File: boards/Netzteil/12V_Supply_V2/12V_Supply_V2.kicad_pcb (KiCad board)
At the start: 2 copper layers, 90 x 66 mm, 52 parts, among them P1 12V_AC, P2 12V_DC_1, P3 12V_DC_2, P4 Relais, P5 12V_DC_3, P6 12V_DC_4, P7 Relais, Q1 BS170, U1 LM393, U2 LM7812CT

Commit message: Added Power LEDs
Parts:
- added D12: LED, LED_THT:LED_D3.0mm, F.Cu at (167.9, 58.7)
- added R2: 47k, Resistor_THT:R_Axial_DIN0207_L6.3mm_D2.5mm_P10.16mm_Horizontal, F.Cu at (162.6, 62.5)
- moved C1 4.83 mm to (140.7, 68.1)
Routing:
- net Net-(D12-Pad2): track 0.00 -> 7.80 mm
- net +12V: track 147.7 -> 154.8 mm
- net GND: vias 29 -> 28
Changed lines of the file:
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@@
     (thickness 1.6)
     (drawings 7)
-    (tracks 155)
+    (tracks 159)
     (zones 0)
-    (modules 52)
-    (nets 19)
+    (modules 54)
+    (nets 20)
   )
   (page A4)
@@
   )
   (setup
-    (last_trace_width 0.5)
+    (last_trace_width 1)
     (user_trace_width 0.5)
     (user_trace_width 1)
@@
   (net 17 "Net-(C10-Pad2)")
   (net 18 "Net-(C11-Pad2)")
+  (net 19 "Net-(D12-Pad2)")
   (net_class Default "Dies ist die voreingestellte Netzklasse."
     (clearance 0.2)
@@
     (add_net "Net-(C4-Pad1)")
     (add_net "Net-(C7-Pad1)")
+    (add_net "Net-(D12-Pad2)")
     (add_net "Net-(D3-Pad1)")
     (add_net "Net-(D5-Pad1)")
@@
     (diff_pair_gap 0.25)
   )
+  (module Resistor_THT:R_Axial_DIN0207_L6.3mm_D2.5mm_P10.16mm_Horizontal (layer F.Cu)
+    (at 162.56 62.484 90)
+    (descr "Resistor, Axial_DIN0207 series, Axial, Horizontal, pin pitch=10.16mm, 0.25W = 1/4W, length*diameter=6.3*2.5mm^2, http://cdn-reichelt.de/documents/datenblatt/B400/1_4W%23YAG.pdf")
+    (tags "Resistor Axial_DIN0207 series Axial Horizontal pin pitch 10.16mm 0.25W = 1/4W length 6.3mm diameter 2.5mm")
+    (fp_text reference R2 (at 5.08 -2.37 90) (layer F.SilkS)
+      (effects (font (size 1 1) (thickness 0.15)))
+    )
+    (fp_text value 47k (at 5.08 2.37 90) (layer F.Fab)
+      (effects (font (size 1 1) (thickness 0.15)))
+    )
+    (fp_text user %R (at 5.08 0 90) (layer F.Fab)
+      (effects (font (size 1 1) (thickness 0.15)))
+    )
+    (fp_line (start 11.21 -1.5) (end -1.05 -1.5) (layer F.CrtYd) (width 0.05))
+    (fp_line (start 11.21 1.5) (end 11.21 -1.5) (layer F.CrtYd) (width 0.05))
+    (fp_line (start -1.05 1.5) (end 11.21 1.5) (layer F.CrtYd) (width 0.05))
+    (fp_line (start -1.05 -1.5) (end -1.05 1.5) (layer F.CrtYd) (width 0.05))
+    (fp_line (start 9.12 0) (end 8.35 0) (layer F.SilkS) (width 0.12))
+    (fp_line (start 1.04 0) (end 1.81 0) (layer F.SilkS) (width 0.12))
+    (fp_line (start 8.35 -1.37) (end 1.81 -1.37) (layer F.SilkS) (width 0.12))
+    (fp_line (start 8.35 1.37) (end 8.35 -1.37) (layer F.SilkS) (width 0.12))
+    (fp_line (start 1.81 1.37) (end 8.35 1.37) (layer F.SilkS) (width 0.12))
+    (fp_line (start 1.81 -1.37) (end 1.81 1.37) (layer F.SilkS) (width 0.12))
+    (fp_line (start 10.16 0) (end 8.23 0) (layer F.Fab) (width 0.1))
+    (fp_line (start 0 0) (end 1.93 0) (layer F.Fab) (width 0.1))
+    (fp_line (start 8.23 -1.25) (end 1.93 -1.25) (layer F.Fab) (width 0.1))
+    (fp_line (start 8.23 1.25) (end 8.23 -1.25) (layer F.Fab) (width 0.1))
+    (fp_line (start 1.93 1.25) (end 8.23 1.25) (layer F.Fab) (width 0.1))
+    (fp_line (start 1.93 -1.25) (end 1.93 1.25) (layer F.Fab) (width 0.1))
+    (pad 2 thru_hole oval (at 10.16 0 90) (size 1.6 1.6) (drill 0.8) (layers *.Cu *.Mask)
+      (net 19 "Net-(D12-Pad2)"))
+    (pad 1 thru_hole circle (at 0 0 90) (size 1.6 1.6) (drill 0.8) (layers *.Cu *.Mask)
+      (net 3 +12V))
+    (model ${KISYS3DMOD}/Resistor_THT.3dshapes/R_Axial_DIN0207_L6.3mm_D2.5mm_P10.16mm_Horizontal.wrl
+      (at (xyz 0 0 0))
+      (scale (xyz 1 1 1))
+      (rotate (xyz 0 0 0))
+    )
+  )
+  (module LED_THT:LED_D3.0mm (layer F.Cu)
+    (at 167.894 58.674 90)
+    (descr "LED, diameter 3.0mm, 2 pins")
+    (tags "LED diameter 3.0mm 2 pins")
+    (fp_text reference D12 (at 1.27 -2.96 90) (layer F.SilkS)
+      (effects (font (size 1 1) (thickness 0.15)))
+    )
+    (fp_text value LED (at 1.27 2.96 90) (layer F.Fab)
+      (effects (font (size 1 1) (thickness 0.15)))
+    )
+    (fp_line (start 3.7 -2.25) (end -1.15 -2.25) (layer F.CrtYd) (width 0.05))
+    (fp_line (start 3.7 2.25) (end 3.7 -2.25) (layer F.CrtYd) (width 0.05))
+    (fp_line (start -1.15 2.25) (end 3.7 2.25) (layer F.CrtYd) (width 0.05))
+    (fp_line (start -1.15 -2.25) (end -1.15 2.25) (layer F.CrtYd) (width 0.05))
+    (fp_line (start -0.29 1.08) (end -0.29 1.236) (layer F.SilkS) (width 0.12))
+    (fp_line (start -0.29 -1.236) (end -0.29 -1.08) (layer F.SilkS) (width 0.12))
+    (fp_line (start -0.23 -1.16619) (end -0.23 1.16619) (layer F.Fab) (width 0.1))
+    (fp_circle (center 1.27 0) (end 2.77 0) (layer F.Fab) (width 0.1))
+    (fp_arc (start 1.27 0) (end 0.229039 1.08) (angle -87.9) (layer F.SilkS) (width 0.12))
+    (fp_arc (start 1.27 0) (end 0.229039 -1.08) (angle 87.9) (layer F.SilkS) (width 0.12))
+    (fp_arc (start 1.27 0) (end -0.29 1.235516) (angle -108.8) (layer F.SilkS) (width 0.12))
+    (fp_arc (start 1.27 0) (end -0.29 -1.235516) (angle 108.8) (layer F.SilkS) (width 0.12))
+    (fp_arc (start 1.27 0) (end -0.23 -1.16619) (angle 284.3) (layer F.Fab) (width 0.1))
+    (pad 2 thru_hole circle (at 2.54 0 90) (size 1.8 1.8) (drill 0.9) (layers *.Cu *.Mask)
+      (net 19 "Net-(D12-Pad2)"))
+    (pad 1 thru_hole rect (at 0 0 90) (size 1.8 1.8) (drill 0.9) (layers *.Cu *.Mask)
+      (net 2 GND))
+    (model ${KISYS3DMOD}/LED_THT.3dshapes/LED_D3.0mm.wrl
+      (at (xyz 0 0 0))
+      (scale (xyz 1 1 1))
+      (rotate (xyz 0 0 0))
+    )
+  )
   (module Loewe:Loewe_Klein (layer F.Cu)
     (at 135.128 55.118)
@@
   )
   (module Capacitor_THT:CP_Radial_D16.0mm_P7.50mm (layer F.Cu)
-    (at 135.89 67.818 270)
+    (at 140.716 68.072 270)
     (descr "CP, Radial series, Radial, pin pitch=7.50mm, , diameter=16mm, Electrolytic Capacitor")
     (tags "CP Radial series Radial pin pitch 7.50mm  diameter 16mm Electrolytic Capacitor")
@@
   (gr_line (start 180.17 113.228) (end 180.17 47.228) (layer Edge.Cuts) (width 0.15))
   (gr_line (start 90.17 113.228) (end 180.17 113.228) (layer Edge.Cuts) (width 0.15))
-  (segment (start 142.748 67.818) (end 148.082 62.484) (width 1) (layer B.Cu) (net 1))
-  (segment (start 135.89 67.818) (end 142.748 67.818) (width 1) (layer B.Cu) (net 1))
   (segment (start 149.352 61.214) (end 148.082 62.484) (width 1) (layer B.Cu) (net 1))
   (segment (start 149.352 58.928) (end 149.352 61.214) (width 1) (layer B.Cu) (net 1))
@@
   (segment (start 149.352 51.748) (end 148.658 51.054) (width 1) (layer B.Cu) (net 1))
   (segment (start 149.352 58.928) (end 149.352 51.748) (width 1) (layer B.Cu) (net 1))
-  (segment (start 135.89 64.77) (end 135.89 67.818) (width 2) (layer B.Cu) (net 1))
-  (segment (start 124.968 60.198) (end 131.318 60.198) (width 2) (layer B.Cu) (net 1))
-  (segment (start 131.318 60.198) (end 135.89 64.77) (width 2) (layer B.Cu) (net 1))
+  (segment (start 140.716 65.872) (end 140.716 68.072) (width 1) (layer B.Cu) (net 1))
+  (segment (start 144.104 62.484) (end 140.716 65.872) (width 1) (layer B.Cu) (net 1))
+  (segment (start 148.082 62.484) (end 144.104 62.484) (width 1) (layer B.Cu) (net 1))
+  (segment (start 129.032 60.198) (end 124.968 60.198) (width 2) (layer B.Cu) (net 1))
+  (segment (start 140.716 68.072) (end 136.906 68.072) (width 2) (layer B.Cu) (net 1))
+  (segment (start 136.906 68.072) (end 129.032 60.198) (width 2) (layer B.Cu) (net 1))
   (via (at 110.49 66.04) (size 1) (drill 0.8) (layers F.Cu B.Cu) (net 2))
   (via (at 114.3 66.04) (size 1) (drill 0.8) (layers F.Cu B.Cu) (net 2))
@@
   (via (at 129.286 51.054) (size 1) (drill 0.8) (layers F.Cu B.Cu) (net 2))
   (via (at 139.446 51.054) (size 1) (drill 0.8) (layers F.Cu B.Cu) (net 2))
-  (via (at 165.608 51.054) (size 1) (drill 0.8) (layers F.Cu B.Cu) (net 2))
   (via (at 177.546 95.25) (size 1) (drill 0.8) (layers F.Cu B.Cu) (net 2))
   (via (at 129.286 63.754) (size 1) (drill 0.8) (layers F.Cu B.Cu) (net 2))
@@
   (via (at 106.172 109.22) (size 1) (drill 0.8) (layers F.Cu B.Cu) (net 2))
   (via (at 106.172 99.568) (size 1) (drill 0.8) (layers F.Cu B.Cu) (net 2))
-  (via (at 165.608 59.182) (size 1) (drill 0.8) (layers F.Cu B.Cu) (net 2))
   (via (at 139.954 59.182) (size 1) (drill 0.8) (layers F.Cu B.Cu) (net 2))
+  (via (at 167.894 51.054) (size 1) (drill 0.8) (layers F.Cu B.Cu) (net 2))
   (segment (start 135.255 97.409) (end 135.255 94.234) (width 0.5) (layer B.Cu) (net 3) (status 30))
   (segment (start 135.255 92.837) (end 135.255 94.234) (width 0.5) (layer B.Cu) (net 3) (status 20))
@@
   (segment (start 159.766 83.185) (end 159.766 83.058) (width 0.5) (layer B.Cu) (net 3))
   (segment (start 159.766 83.058) (end 163.322 83.058) (width 0.5) (layer B.Cu) (net 3))
+  (segment (start 155.448 62.484) (end 162.56 62.484) (width 0.5) (layer B.Cu) (net 3))
   (segment (start 112.776 105.029) (end 116.332 105.029) (width 0.5) (layer B.Cu) (net 4) (status 30))
   (segment (start 116.332 105.029) (end 119.888 105.029) (width 0.5) (layer B.Cu) (net 4) (status 30))
@@
   (segment (start 114.808 77.256) (end 117.562 77.256) (width 2) (layer F.Cu) (net 18))
   (segment (start 117.562 77.256) (end 119.126 75.692) (width 2) (layer F.Cu) (net 18))
+  (segment (start 162.56 53.848) (end 162.56 52.324) (width 0.5) (layer B.Cu) (net 19))
+  (segment (start 167.894 56.134) (end 164.846 56.134) (width 0.5) (layer B.Cu) (net 19))
+  (segment (start 164.846 56.134) (end 162.56 53.848) (width 0.5) (layer B.Cu) (net 19))
   (zone (net 2) (net_name GND) (layer B.Cu) (hatch edge 0.508)
     (connect_pads (clearance 0.5))

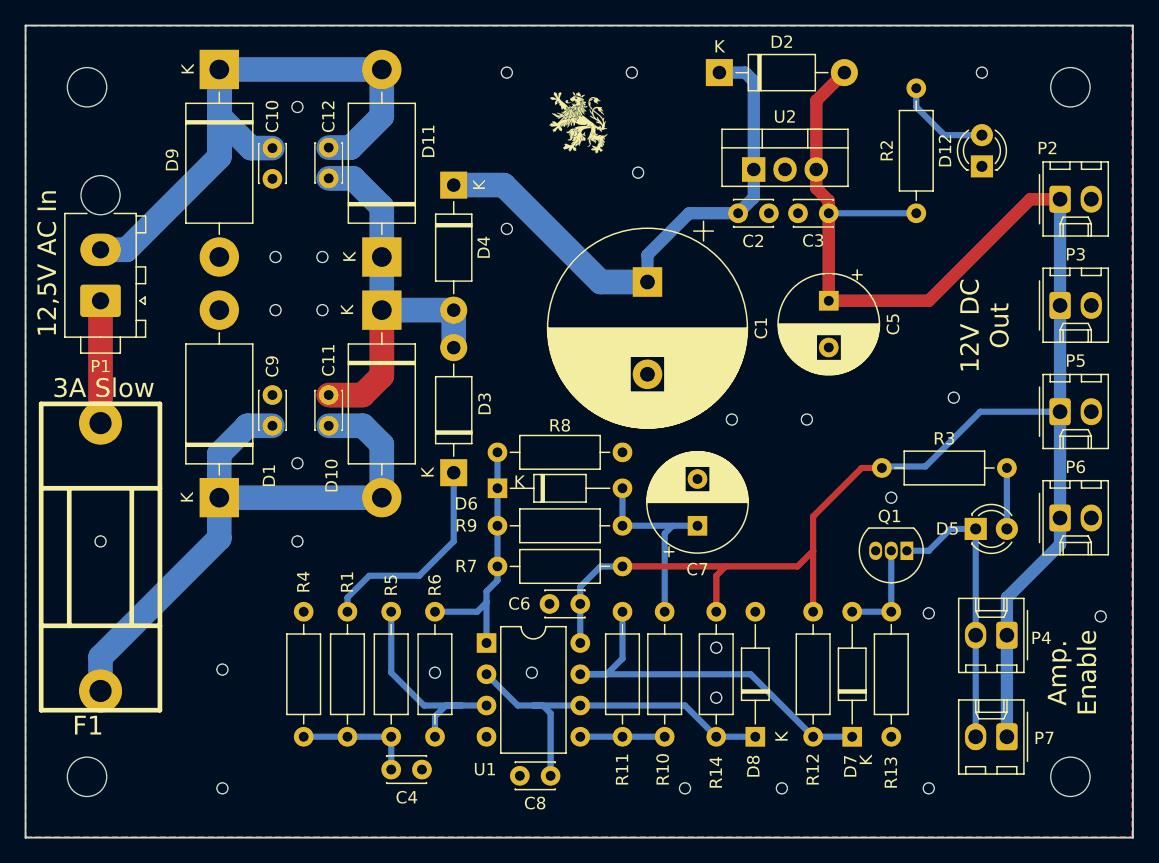
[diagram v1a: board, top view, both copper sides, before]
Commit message: Adjusted Silkscreen
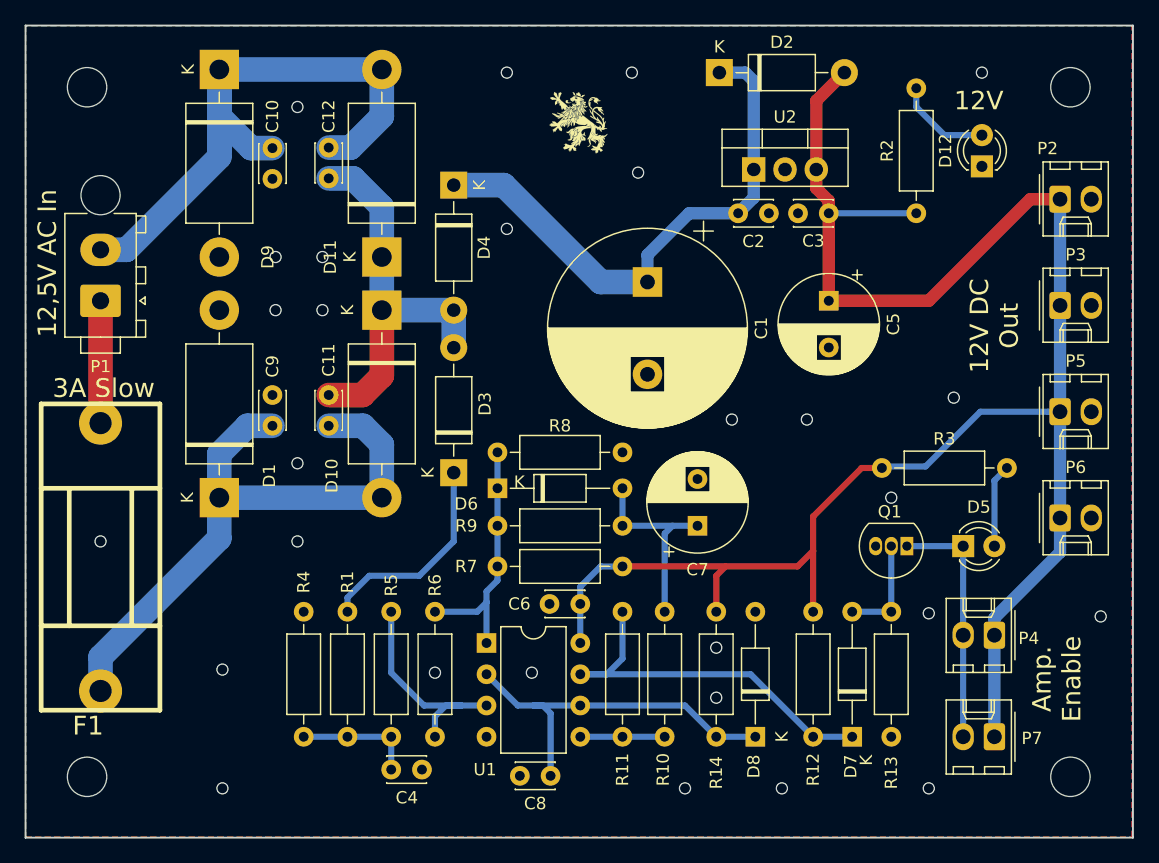
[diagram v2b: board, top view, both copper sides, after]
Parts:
- moved D5 1.73 mm to (166.4, 89.5)
- moved P4 1.02 mm to (168.9, 96.8)
- moved P7 1.02 mm to (168.9, 105.0)
- moved Q1 0.38 mm to (161.8, 89.5)
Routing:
- net Net-(D5-Pad1): track 23.2 -> 20.1 mm
- net Net-(D5-Pad2): track 4.95 -> 6.77 mm
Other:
- board text added: "12V"
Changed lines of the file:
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@@
   (general
     (thickness 1.6)
-    (drawings 7)
-    (tracks 159)
+    (drawings 8)
+    (tracks 160)
     (zones 0)
     (modules 54)
@@
   (page A4)
   (layers
-    (0 F.Cu jumper)
-    (31 B.Cu signal)
+    (0 F.Cu jumper hide)
+    (31 B.Cu signal hide)
     (32 B.Adhes user)
     (33 F.Adhes user)
@@
   )
   (setup
-    (last_trace_width 1)
+    (last_trace_width 0.5)
     (user_trace_width 0.5)
     (user_trace_width 1)
@@
     (descr "Diode, DO-201AD series, Axial, Horizontal, pin pitch=15.24mm, , length*diameter=9.5*5.2mm^2, , http://www.diodes.com/_files/packages/DO-201AD.pdf")
     (tags "Diode DO-201AD series Axial Horizontal pin pitch 15.24mm  length 9.5mm diameter 5.2mm")
-    (fp_text reference D11 (at 9.398 3.81 90) (layer F.SilkS)
+    (fp_text reference D11 (at 0 -4.191 90) (layer F.SilkS)
       (effects (font (size 1 1) (thickness 0.15)))
     )
@@
     (descr "Diode, DO-201AD series, Axial, Horizontal, pin pitch=15.24mm, , length*diameter=9.5*5.2mm^2, , http://www.diodes.com/_files/packages/DO-201AD.pdf")
     (tags "Diode DO-201AD series Axial Horizontal pin pitch 15.24mm  length 9.5mm diameter 5.2mm")
-    (fp_text reference D9 (at 7.366 3.81 90) (layer F.SilkS)
+    (fp_text reference D9 (at 15.24 -3.937 90) (layer F.SilkS)
       (effects (font (size 1 1) (thickness 0.15)))
     )
@@
   )
   (module Package_TO_SOT_THT:TO-92_Inline (layer F.Cu)
-    (at 161.798 89.916 180)
+    (at 161.798 89.535 180)
     (descr "TO-92 leads in-line, narrow, oval pads, drill 0.75mm (see NXP sot054_po.pdf)")
     (tags "to-92 sc-43 sc-43a sot54 PA33 transistor")
@@
   )
   (module Connector_Molex:Molex_KK-254_AE-6410-02A_1x02_P2.54mm_Vertical (layer F.Cu)
-    (at 169.926 105.029 180)
+    (at 168.91 105.029 180)
     (descr "Molex KK-254 Interconnect System, old/engineering part number: AE-6410-02A example for new part number: 22-27-2021, 2 Pins (http://www.molex.com/pdm_docs/sd/022272021_sd.pdf), generated with kicad-footprint-generator")
     (tags "connector Molex KK-254 side entry")
@@
   )
   (module Connector_Molex:Molex_KK-254_AE-6410-02A_1x02_P2.54mm_Vertical (layer F.Cu)
-    (at 169.926 96.774 180)
+    (at 168.91 96.774 180)
     (descr "Molex KK-254 Interconnect System, old/engineering part number: AE-6410-02A example for new part number: 22-27-2021, 2 Pins (http://www.molex.com/pdm_docs/sd/022272021_sd.pdf), generated with kicad-footprint-generator")
     (tags "connector Molex KK-254 side entry")
@@
   )
   (module LED_THT:LED_D3.0mm (layer F.Cu)
-    (at 167.386 88.138)
+    (at 166.37 89.535)
     (descr "LED, diameter 3.0mm, 2 pins")
     (tags "LED diameter 3.0mm 2 pins")
-    (fp_text reference D5 (at -2.286 0) (layer F.SilkS)
+    (fp_text reference D5 (at 1.27 -3.175) (layer F.SilkS)
       (effects (font (size 1 1) (thickness 0.15)))
     )
@@
     )
   )
+  (gr_text 12V (at 167.64 53.34) (layer F.SilkS)
+    (effects (font (size 1.5 1.5) (thickness 0.3)))
+  )
   (gr_text "12,5V AC In" (at 91.948 66.548 90) (layer F.SilkS)
     (effects (font (size 1.5 1.5) (thickness 0.3)))
   )
-  (gr_text "12V DC\nOut" (at 168.148 71.628 90) (layer F.SilkS)
+  (gr_text "12V DC\nOut" (at 168.91 71.628 90) (layer F.SilkS)
     (effects (font (size 1.5 1.5) (thickness 0.3)))
   )
-  (gr_text "Amp.\nEnable" (at 175.26 99.822 90) (layer F.SilkS)
+  (gr_text "Amp.\nEnable" (at 173.99 100.33 90) (layer F.SilkS)
     (effects (font (size 1.5 1.5) (thickness 0.3)))
   )
@@
   (segment (start 155.448 62.484) (end 155.448 61.468) (width 1) (layer F.Cu) (net 3))
   (segment (start 155.448 61.468) (end 154.432 60.452) (width 1) (layer F.Cu) (net 3))
-  (segment (start 169.926 105.029) (end 169.926 96.774) (width 1) (layer B.Cu) (net 3))
   (segment (start 174.244 87.249) (end 174.244 61.341) (width 1) (layer B.Cu) (net 3))
-  (segment (start 169.926 93.726) (end 169.926 96.774) (width 1) (layer B.Cu) (net 3))
-  (segment (start 174.244 87.249) (end 174.244 89.408) (width 1) (layer B.Cu) (net 3))
-  (segment (start 174.244 89.408) (end 169.926 93.726) (width 1) (layer B.Cu) (net 3))
   (segment (start 171.831 61.341) (end 174.244 61.341) (width 1) (layer F.Cu) (net 3))
   (segment (start 155.448 69.596) (end 163.576 69.596) (width 1) (layer F.Cu) (net 3))
@@
   (segment (start 159.766 83.058) (end 163.322 83.058) (width 0.5) (layer B.Cu) (net 3))
   (segment (start 155.448 62.484) (end 162.56 62.484) (width 0.5) (layer B.Cu) (net 3))
+  (segment (start 168.91 105.029) (end 168.91 96.774) (width 1) (layer B.Cu) (net 3))
+  (segment (start 174.244 90.043) (end 174.244 87.249) (width 1) (layer B.Cu) (net 3))
+  (segment (start 168.91 96.774) (end 168.91 95.377) (width 1) (layer B.Cu) (net 3))
+  (segment (start 168.91 95.377) (end 174.244 90.043) (width 1) (layer B.Cu) (net 3))
   (segment (start 112.776 105.029) (end 116.332 105.029) (width 0.5) (layer B.Cu) (net 4) (status 30))
   (segment (start 116.332 105.029) (end 119.888 105.029) (width 0.5) (layer B.Cu) (net 4) (status 30))
   (segment (start 119.888 107.696) (end 119.888 105.029) (width 0.5) (layer B.Cu) (net 4) (status 30))
   (segment (start 96.266 79.5401) (end 96.266 69.596) (width 2) (layer F.Cu) (net 5))
-  (segment (start 169.926 88.138) (end 169.926 83.185) (width 0.5) (layer B.Cu) (net 6) (status 30))
+  (segment (start 168.91 84.201) (end 169.926 83.185) (width 0.5) (layer B.Cu) (net 6))
+  (segment (start 168.91 89.535) (end 168.91 84.201) (width 0.5) (layer B.Cu) (net 6))
   (segment (start 138.684 84.836) (end 138.684 87.884) (width 0.5) (layer B.Cu) (net 7) (status 30))
   (segment (start 138.684 87.884) (end 142.748 87.884) (width 0.5) (layer B.Cu) (net 7) (status 10))
@@
   (segment (start 124.968 83.566) (end 124.968 89.154) (width 0.5) (layer B.Cu) (net 8) (status 10))
   (segment (start 124.968 89.154) (end 122.174 91.948) (width 0.5) (layer B.Cu) (net 8))
-  (segment (start 163.576 89.916) (end 161.798 89.916) (width 0.5) (layer B.Cu) (net 9))
-  (segment (start 167.386 88.138) (end 165.354 88.138) (width 0.5) (layer B.Cu) (net 9))
-  (segment (start 165.354 88.138) (end 163.576 89.916) (width 0.5) (layer B.Cu) (net 9))
-  (segment (start 167.386 105.029) (end 167.386 88.138) (width 0.5) (layer B.Cu) (net 9))
+  (segment (start 166.37 105.029) (end 166.37 96.774) (width 0.5) (layer B.Cu) (net 9))
+  (segment (start 166.37 95.174) (end 166.37 89.535) (width 0.5) (layer B.Cu) (net 9))
+  (segment (start 166.37 96.774) (end 166.37 95.174) (width 0.5) (layer B.Cu) (net 9))
+  (segment (start 161.798 89.535) (end 166.37 89.535) (width 0.5) (layer B.Cu) (net 9))
   (segment (start 128.524 87.884) (end 128.524 91.186) (width 0.5) (layer B.Cu) (net 10) (status 30))
   (segment (start 126.873 94.869) (end 127.635 94.107) (width 0.5) (layer B.Cu) (net 10))
